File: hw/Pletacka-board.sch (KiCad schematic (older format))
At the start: 37 parts, among them J4 STOP_INPUT, J5 POWER_&_FINN_INPUT

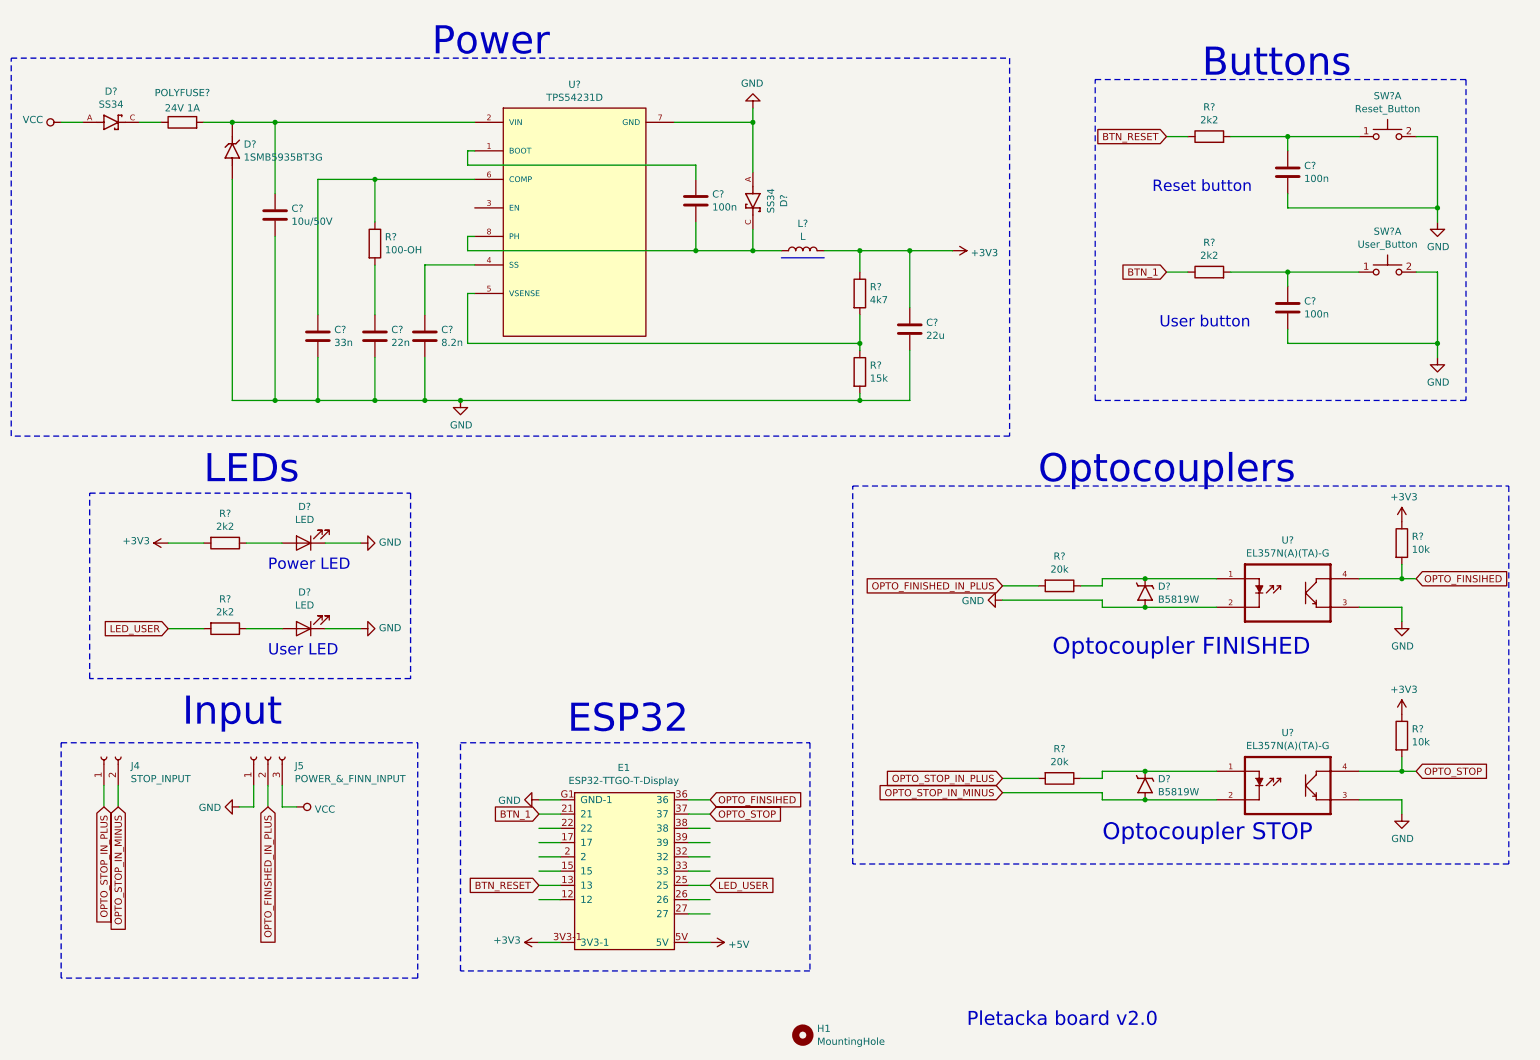
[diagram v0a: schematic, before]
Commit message: Remove blank sheets
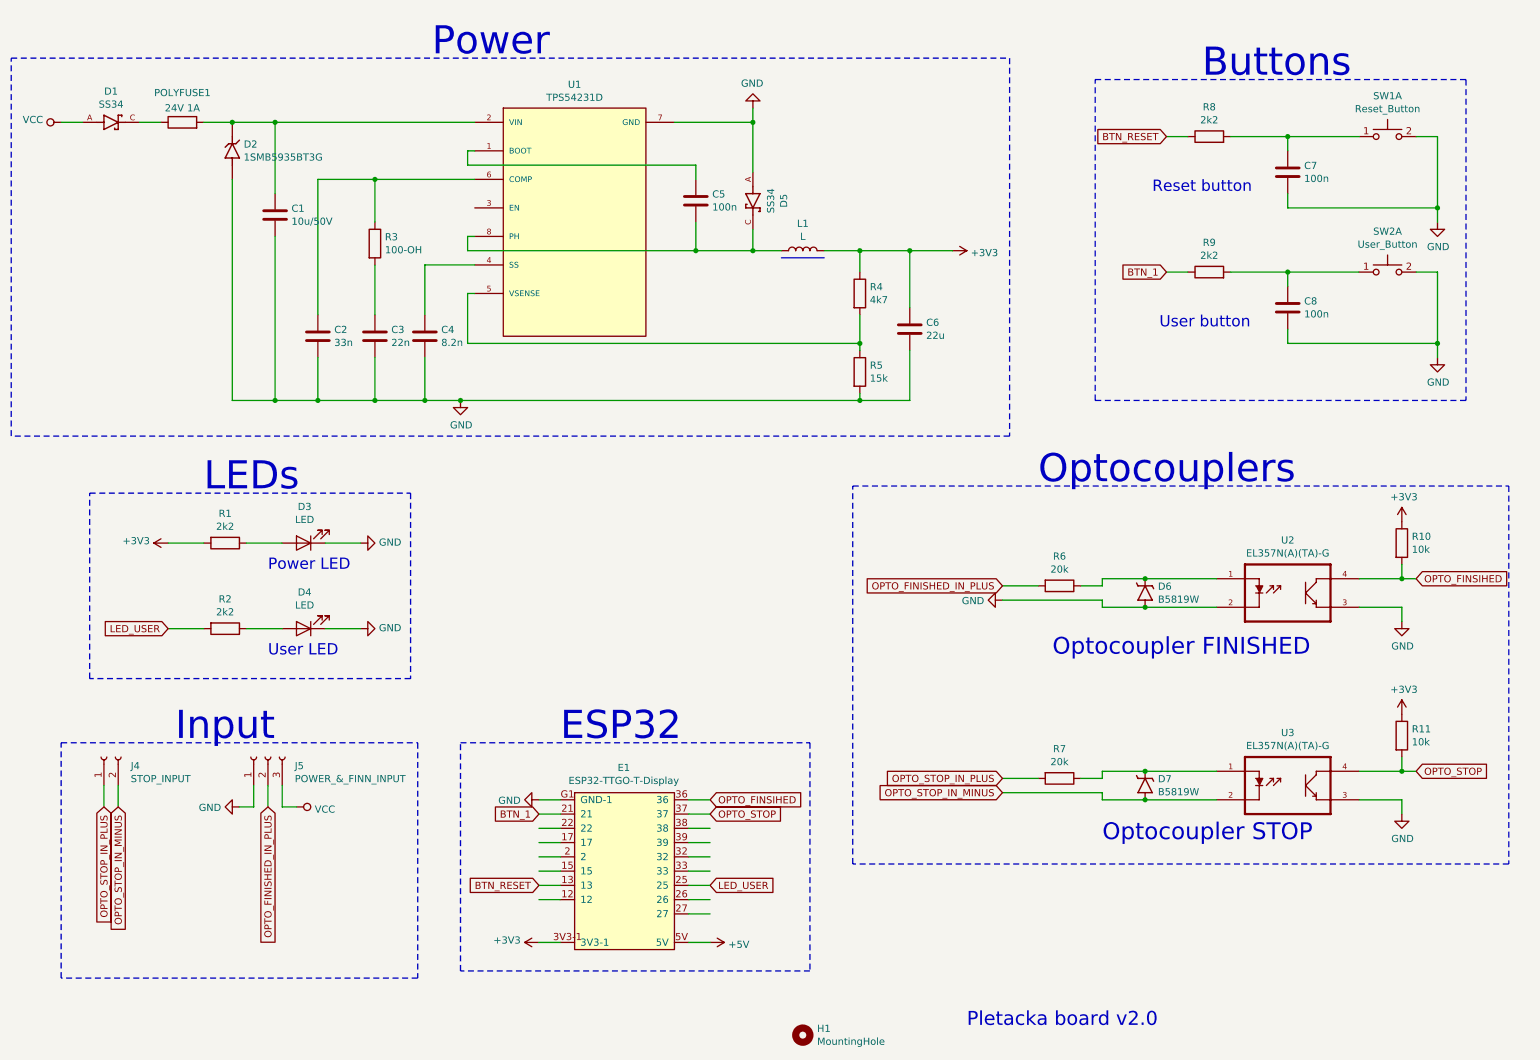
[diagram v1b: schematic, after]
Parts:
- gave numbers to parts that had none: 33

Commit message: Change buttons and fill ground
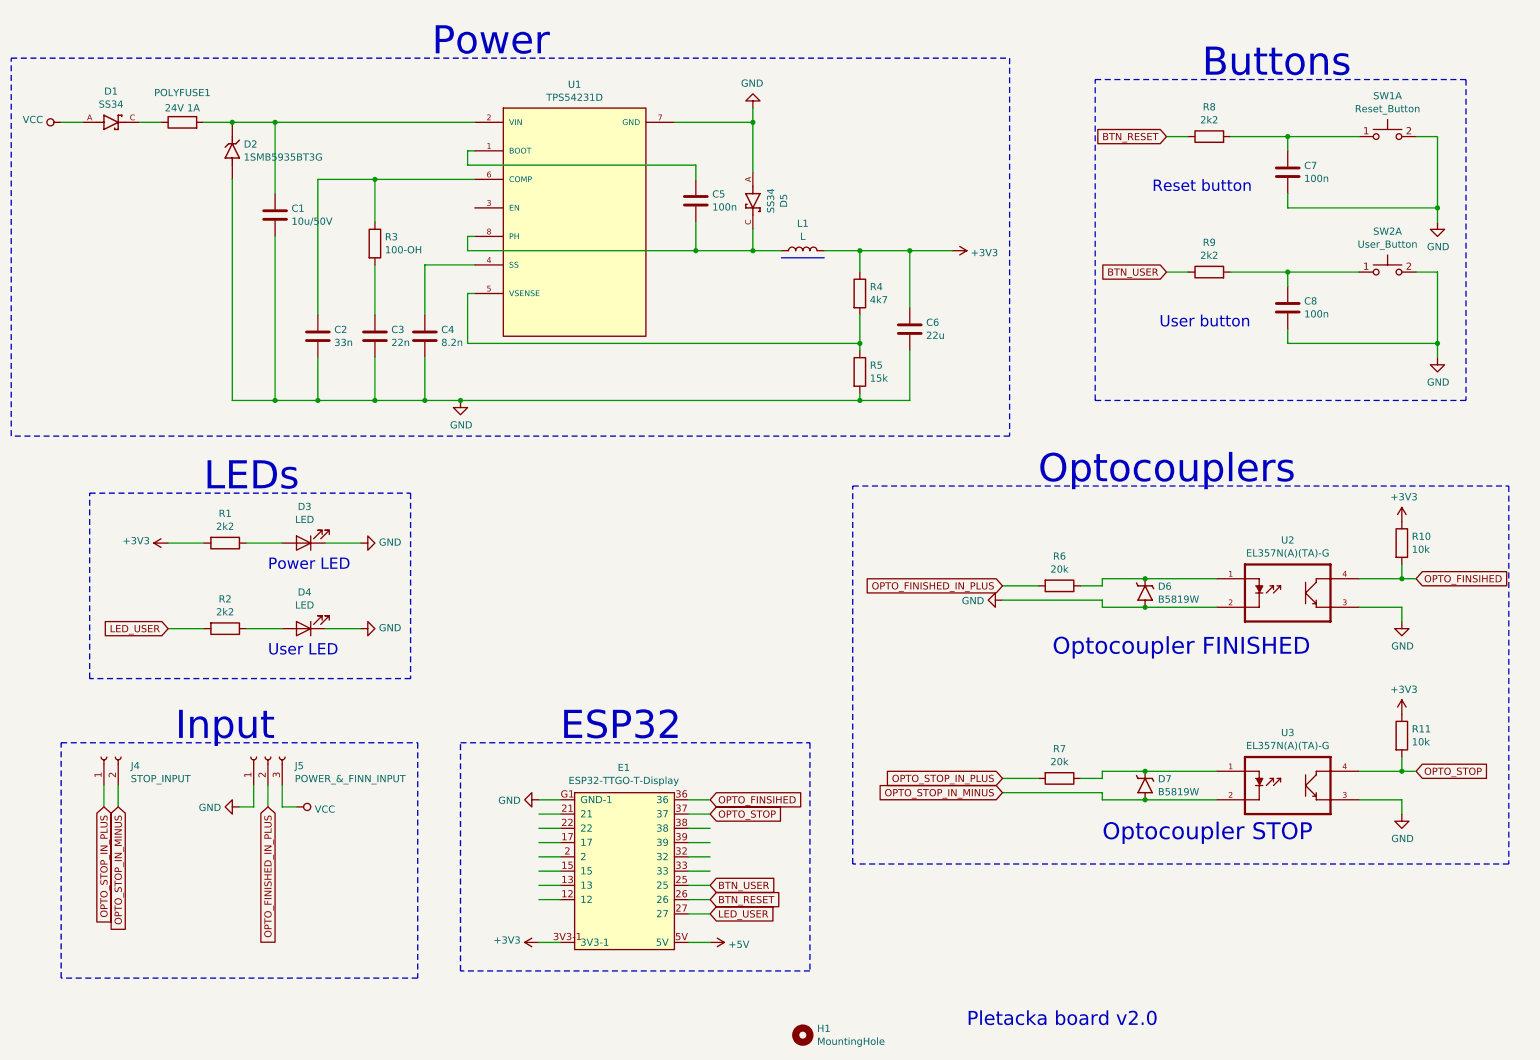
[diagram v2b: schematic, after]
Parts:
- SW1, SW2: footprint Button_SMD:SW_SPST_SKQG_WithStem -> Button_SMD:Button_SMD_10mm
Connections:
- net labels added: BTN_USER
- net labels removed: BTN_1
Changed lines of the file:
@@
 BTN_RESET
 Text GLabel 8750 2250 0    50   Input ~ 0
-BTN_1
+BTN_USER
 Text GLabel 10500 4400 2    50   Input ~ 0
 OPTO_FINSIHED
@@
 F 0 "SW1" H 10300 1585 50  0000 C CNN
 F 1 "Reset_Button" H 10300 1494 50  0000 C CNN
-F 2 "Button_SMD:SW_SPST_SKQG_WithStem" H 10300 1500 50  0001 C CNN
+F 2 "Button_SMD:Button_SMD_10mm" H 10300 1500 50  0001 C CNN
 F 3 "~" H 10300 1500 50  0001 C CNN
 F 4 "C318887" H 10300 1300 50  0001 C CNN "LCSC_ID"
@@
 F 0 "SW2" H 10300 2535 50  0000 C CNN
 F 1 "User_Button" H 10300 2444 50  0000 C CNN
-F 2 "Button_SMD:SW_SPST_SKQG_WithStem" H 10300 2450 50  0001 C CNN
+F 2 "Button_SMD:Button_SMD_10mm" H 10300 2450 50  0001 C CNN
 F 3 "~" H 10300 2450 50  0001 C CNN
 F 4 "C318887" H 10300 2250 50  0001 C CNN "LCSC_ID"
@@
 Wire Notes Line
 	6250 5550 6250 7150
-Text GLabel 5550 6550 2    50   Input ~ 0
+Text GLabel 5550 6750 2    50   Input ~ 0
 LED_USER
 Text Notes 4500 5550 0    197  ~ 0
@@
 Wire Wire Line
 	4500 6150 4350 6150
-Text GLabel 4350 6550 0    50   Input ~ 0
+Text GLabel 5550 6650 2    50   Input ~ 0
 BTN_RESET
-Text GLabel 4350 6050 0    50   Input ~ 0
-BTN_1
+Text GLabel 5550 6550 2    50   Input ~ 0
+BTN_USER
 Wire Wire Line
 	4500 6050 4350 6050

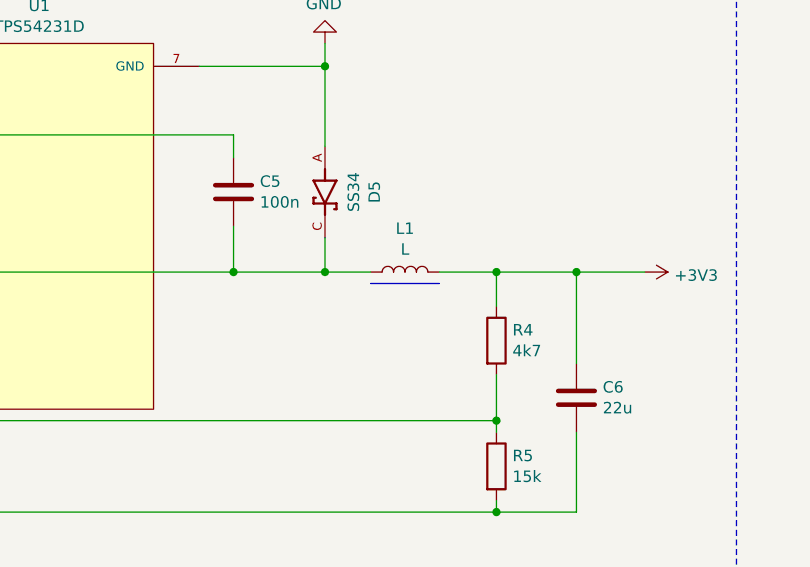
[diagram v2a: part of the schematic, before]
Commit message: Change Inductor
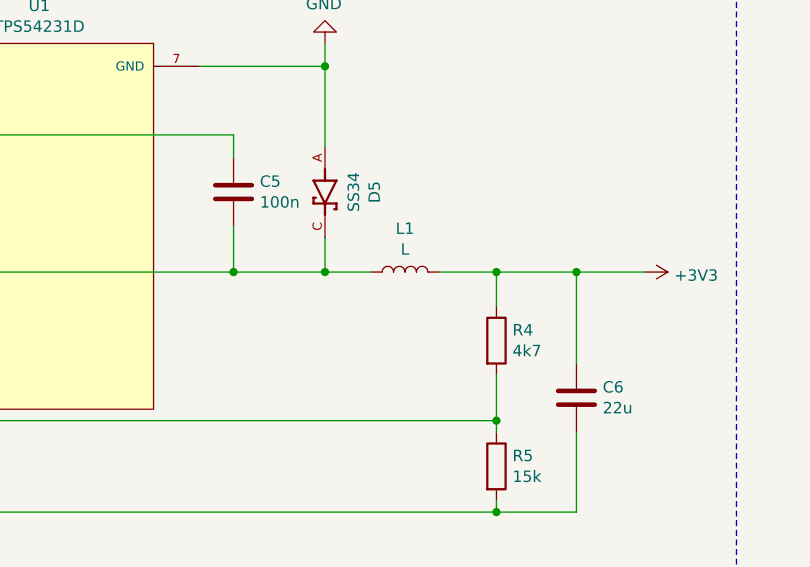
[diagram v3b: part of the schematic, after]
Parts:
- L1: footprint Inductor_SMD:L_TDK_SLF7045 -> SLW6045S220MST:SLW; LCSC_ID (none) -> C206321
- SW1, SW2: LCSC_ID C318887 -> C620322
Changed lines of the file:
@@
 F 2 "Button_SMD:Button_SMD_10mm" H 10300 1500 50  0001 C CNN
 F 3 "~" H 10300 1500 50  0001 C CNN
-F 4 "C318887" H 10300 1300 50  0001 C CNN "LCSC_ID"
+F 4 "C620322" H 10300 1300 50  0001 C CNN "LCSC_ID"
 	1    10300 1300
 	1    0    0    -1
@@
 F 2 "Button_SMD:Button_SMD_10mm" H 10300 2450 50  0001 C CNN
 F 3 "~" H 10300 2450 50  0001 C CNN
-F 4 "C318887" H 10300 2250 50  0001 C CNN "LCSC_ID"
+F 4 "C620322" H 10300 2250 50  0001 C CNN "LCSC_ID"
 	1    10300 2250
 	1    0    0    -1
@@
 F 0 "L1" V 6390 2100 50  0000 C CNN
 F 1 "L" V 6299 2100 50  0000 C CNN
-F 2 "Inductor_SMD:L_TDK_SLF7045" H 6200 2100 50  0001 C CNN
+F 2 "SLW6045S220MST:SLW" H 6200 2100 50  0001 C CNN
 F 3 "~" H 6200 2100 50  0001 C CNN
+F 4 "C206321" V 6200 2100 50  0001 C CNN "LCSC_ID"
 	1    6200 2100
 	0    -1   -1   0
@@
 Wire Wire Line
 	3550 3150 3800 3150
-Wire Bus Line
-	6050 2150 6350 2150
 Connection ~ 3800 3150
 Wire Wire Line
